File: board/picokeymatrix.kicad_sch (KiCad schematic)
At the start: 55 parts, among them CN1 PJ-3220-Y, J1 Conn_01x12, J10 Conn_01x18, J11 Conn_01x04, J12 Conn_01x04, J13 Conn_01x04, J14 Conn_01x04, J15 Conn_01x04, J16 Conn_01x04, J17 Conn_01x04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

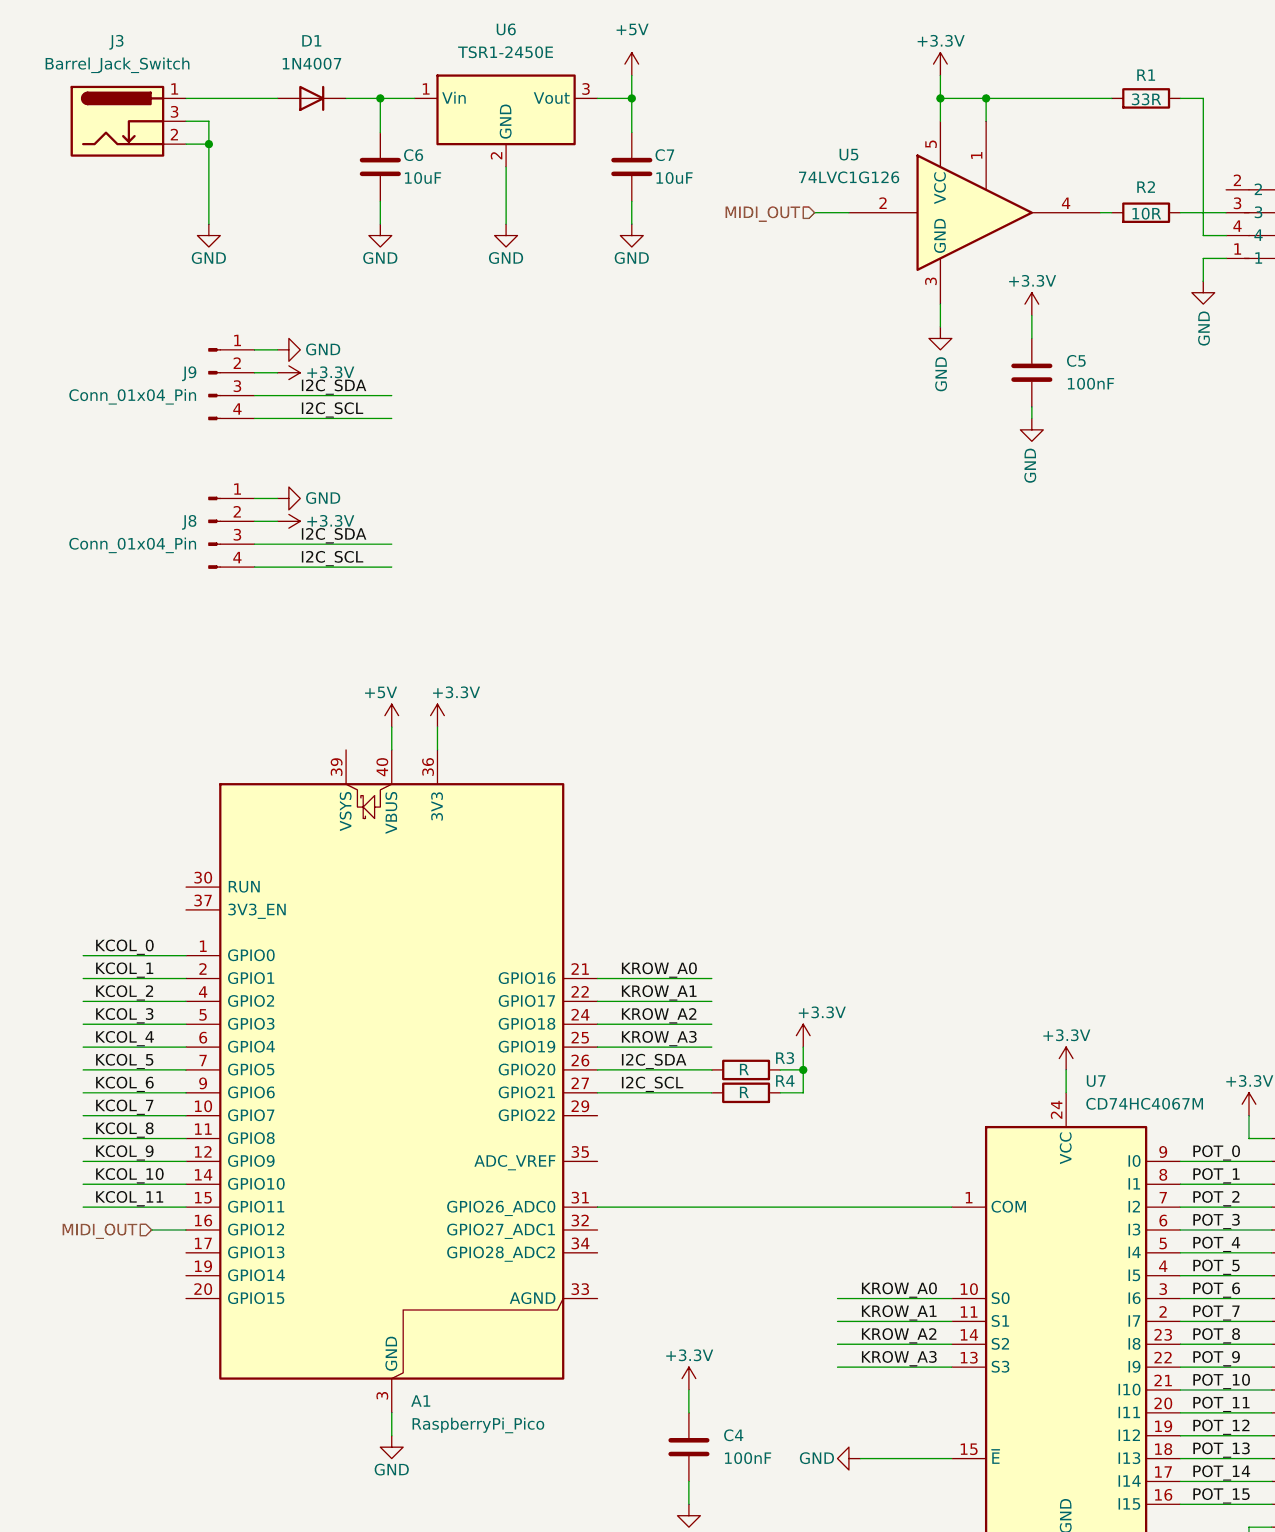
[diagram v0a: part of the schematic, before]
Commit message: Potmeter pinout, caps on supply
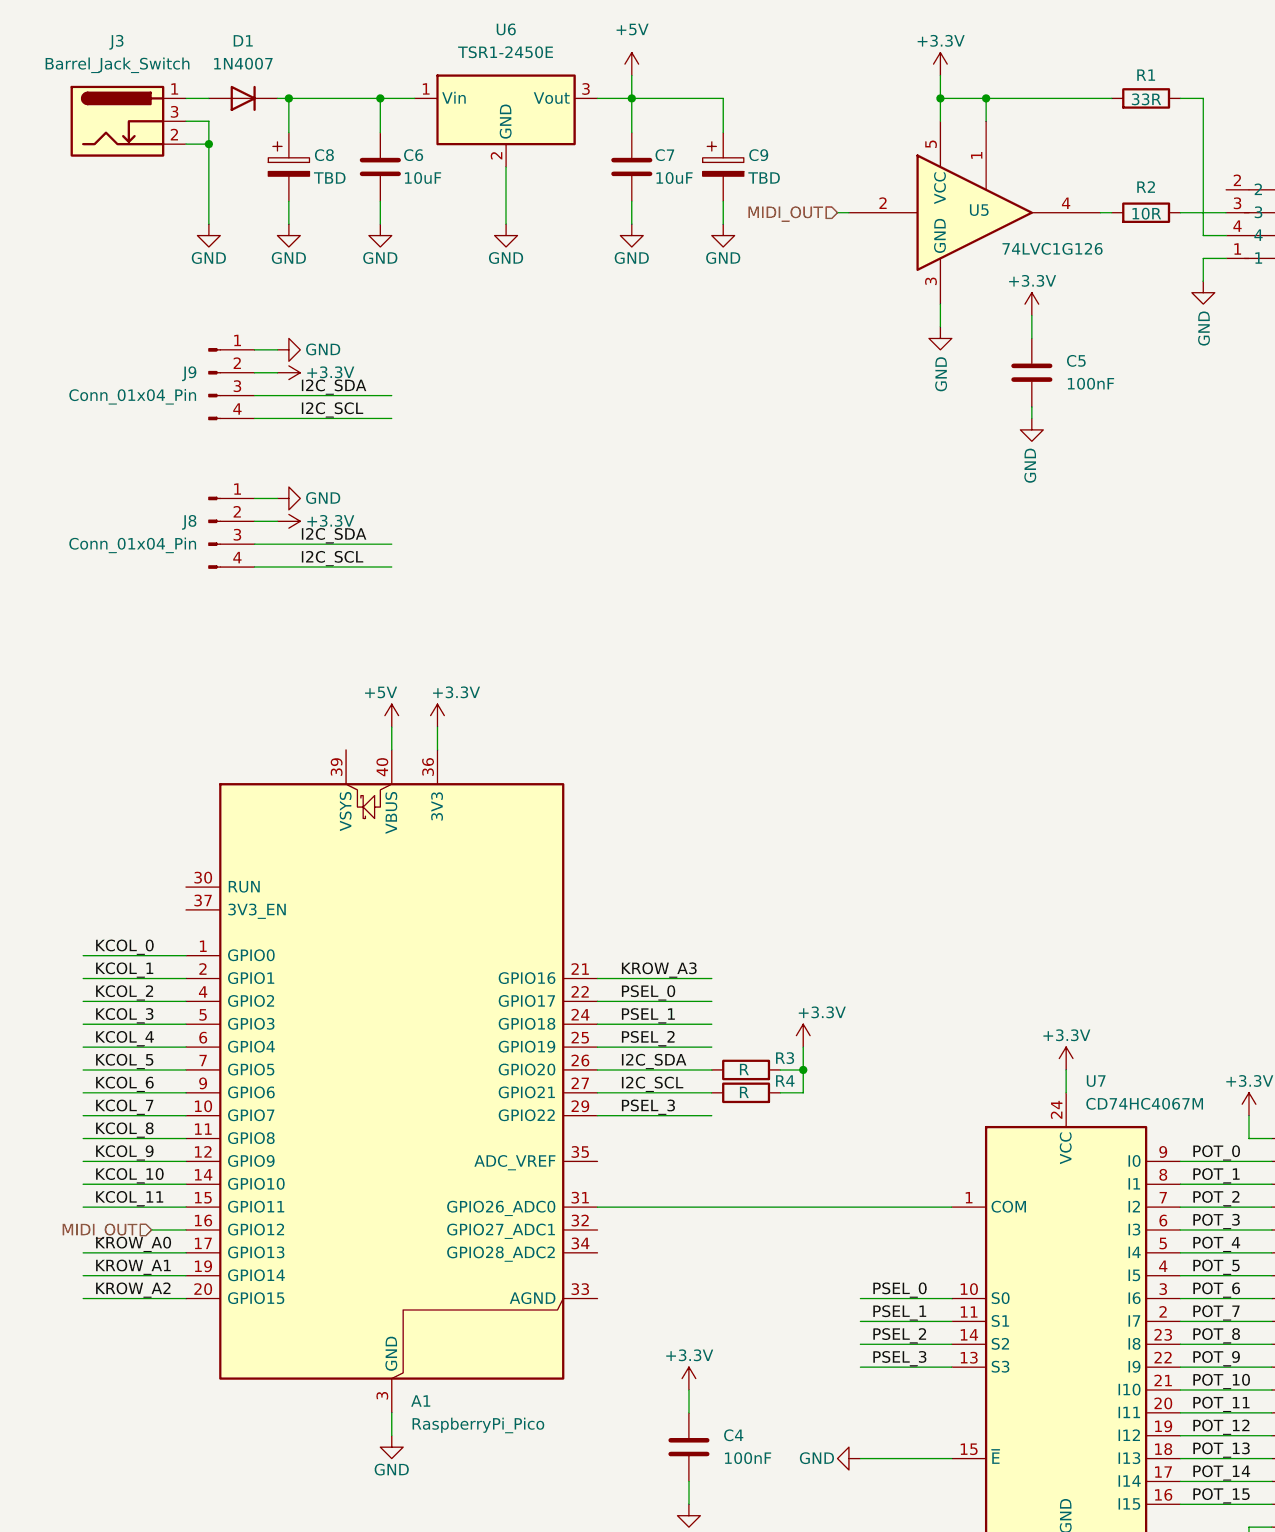
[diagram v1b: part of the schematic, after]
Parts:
- added C8, C9: TBD, C_Radial_D5.0mm_H7.0mm_P2.00mm, symbol Device:C_Polarized
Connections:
- net +5V: now also C9.1
- net GND: now also C8.2, C9.2
- net KROW_A0: now also A1.17 (GPIO13); no longer A1.21 (GPIO16), U7.10 (S0)
- net KROW_A1: now also A1.19 (GPIO14); no longer A1.22 (GPIO17), U7.11 (S1)
- net KROW_A2: now also A1.20 (GPIO15); no longer A1.24 (GPIO18), U7.14 (S2)
- net KROW_A3: now also A1.21 (GPIO16); no longer A1.25 (GPIO19), U7.13 (S3)
- net at C6.1, D1.1 (K), U6.1 (Vin): now also C8.1
- net PSEL_3: now reaches A1.29 (GPIO22)
- net PSEL_3: now also U7.13 (S3)
- new net PSEL_0: A1.22 (GPIO17), U7.10 (S0)
- new net PSEL_1: A1.24 (GPIO18), U7.11 (S1)
- new net PSEL_2: A1.25 (GPIO19), U7.14 (S2)
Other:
- moved on the sheet: D1

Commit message: Fix RPi pico footprint for TH mounting
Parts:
- A1: footprint Module:RaspberryPi_Pico_Common_Unspecified -> Module:RaspberryPi_Pico_Common_THT
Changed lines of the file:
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@@
 			)
 		)
-		(property "Footprint" "Module:RaspberryPi_Pico_Common_Unspecified"
+		(property "Footprint" "Module:RaspberryPi_Pico_Common_THT"
 			(at 52.07 180.34 0)
 			(effects
